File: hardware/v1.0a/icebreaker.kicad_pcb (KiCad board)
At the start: 4 copper layers, 73 x 37 mm, 128 parts, among them J1 Jumper, J10 Jumper, J11 Jumper, J12 Jumper, J13 Jumper, J14 Jumper, J15 Jumper, J16 Jumper, J17 Jumper, J18 Jumper, J19 Jumper, J2 Jumper, J20 Flash, J21 PMOD_1A, J22 PMOD_1B, J23 PMOD_2H, J24 PMOD_2P, J25 RGB Led, J26 5V AUX, J27 5V AUX, J28 CRESET, J3 Jumper, J4 Jumper, J5 Jumper, J6 Jumper, J7 Jumper, J8 Jumper, J9 Jumper, P1 pkl_USB_OTG, P2 UP, P3 UP, P4 UP, P5 UP, SW1 TACT, SW2 TACT, SW3 TACT, SW4 TACT, U1 93C46B-SOT-23-6, U2 3.3V, U3 1V2, U4 FT2232H, U5 W25Q, U6 ICE5LP4K-SG48, U7 12MHz

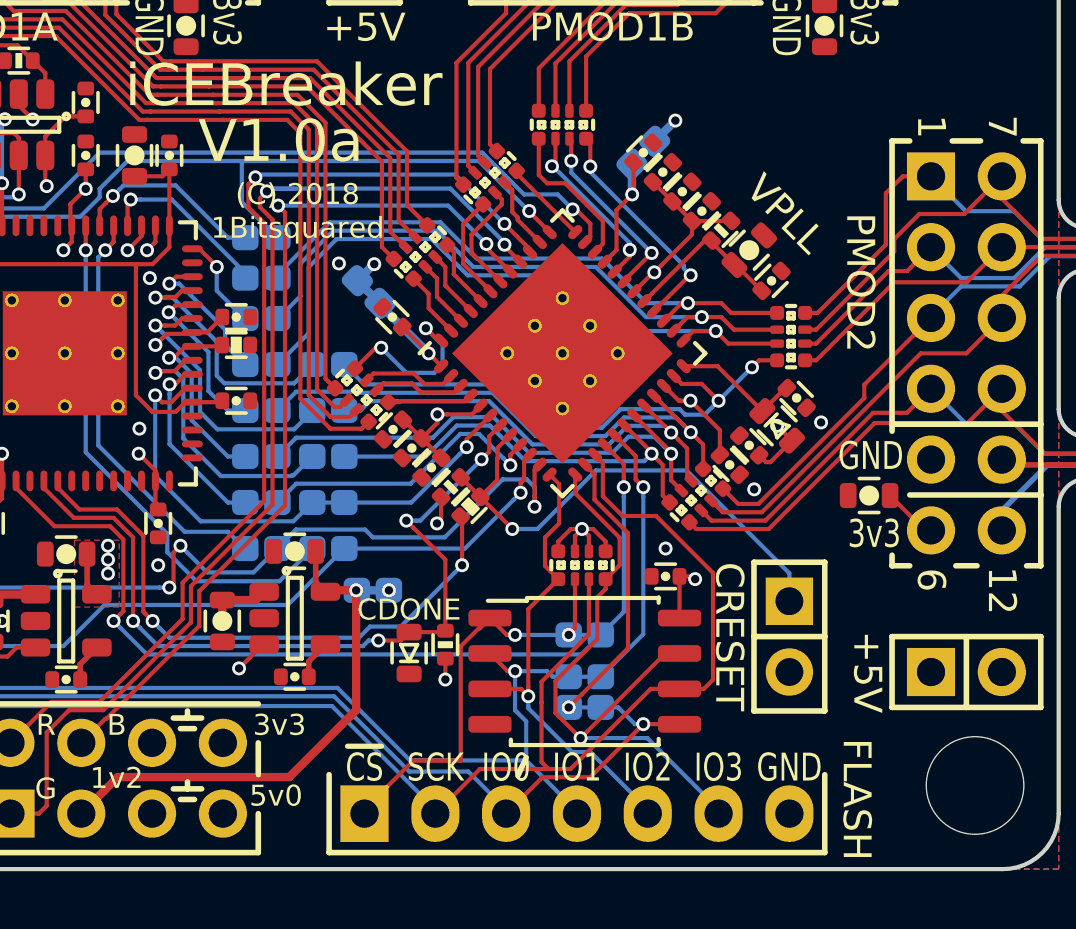
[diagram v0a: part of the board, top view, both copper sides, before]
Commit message: Updated BOM and assembly documentation.
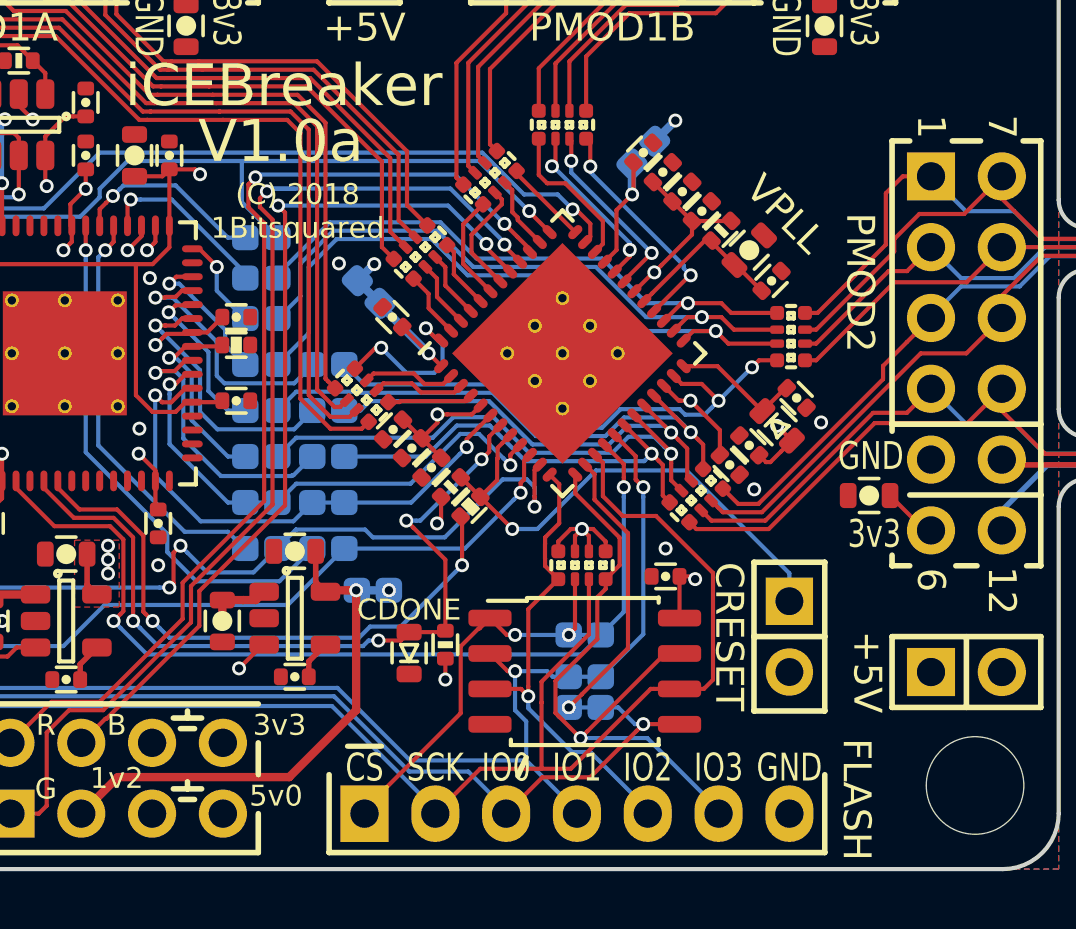
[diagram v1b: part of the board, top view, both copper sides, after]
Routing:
- net +1V8: track 32.5 -> 33.6 mm, vias 0 -> 1
- net /FLASH_CS: track 15.1 -> 14.1 mm

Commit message: Changed the inline CRESET resestor to 2k2.
We need a lower resistor value so that the FTDI chip can reset the FPGA.
Using a 10k resistor results in a voltage divider and the 1.65v is too
high to assert reset.
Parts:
- D3: value GRN -> BLU
- J21: value PMOD_1A -> PMOD
- J22: value PMOD_1B -> PMOD
- J23: value PMOD_2H -> PMOD
- J24: value PMOD_2P -> PMOD
- R26: value 10k -> 2k2
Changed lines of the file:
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@@
       (effects (font (size 1 1) (thickness 0.15)))
     )
-    (fp_text value PMOD_2P (at 2.65 6.35 270) (layer F.Fab)
+    (fp_text value PMOD (at 2.65 6.35 270) (layer F.Fab)
       (effects (font (size 1 1) (thickness 0.15)))
     )
@@
       (effects (font (size 1 1) (thickness 0.15)))
     )
-    (fp_text value PMOD_2H (at 6.45 0.68 90) (layer F.Fab)
+    (fp_text value PMOD (at 6.45 0.68 90) (layer F.Fab)
       (effects (font (size 1 1) (thickness 0.15)))
     )
@@
       (effects (font (size 1 1) (thickness 0.15)))
     )
-    (fp_text value PMOD_1B (at 5.98 0.03 180) (layer F.Fab)
+    (fp_text value PMOD (at 5.98 0.03 180) (layer F.Fab)
       (effects (font (size 1 1) (thickness 0.15)))
     )
@@
       (effects (font (size 1 1) (thickness 0.15)))
     )
-    (fp_text value PMOD_1A (at 6.32 0.03 180) (layer F.Fab)
+    (fp_text value PMOD (at 6.32 0.03 180) (layer F.Fab)
       (effects (font (size 1 1) (thickness 0.15)))
     )
@@
       (effects (font (size 0.635 0.635) (thickness 0.1)))
     )
-    (fp_text value 10k (at -1.838478 0 225) (layer F.Fab)
+    (fp_text value 2k2 (at -1.838478 0 225) (layer F.Fab)
       (effects (font (size 0.635 0.635) (thickness 0.1)))
     )
@@
       (effects (font (size 0.635 0.635) (thickness 0.1)))
     )
-    (fp_text value GRN (at -1.65 0 180) (layer F.Fab)
+    (fp_text value BLU (at -1.65 0 180) (layer F.Fab)
       (effects (font (size 0.5 0.5) (thickness 0.1)))
     )

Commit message: Fixed pin header 3d models.
We had some of the models doubled up or not fully disabled. Now the TH
pin headers are all using KiCad V5 3d model locations and are all
disabled.

This fixes #23
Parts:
- removed the REF** at (42.2, 47.2)
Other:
- board text removed: "1Bitsquared"
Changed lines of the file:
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@@
-(kicad_pcb (version 20171130) (host pcbnew 5.0.0-fee4fd1~66~ubuntu18.04.1)
+(kicad_pcb (version 20171130) (host pcbnew 5.1.2-f72e74a~84~ubuntu18.04.1)
   (general
     (thickness 1.6)
-    (drawings 335)
+    (drawings 334)
     (tracks 1467)
     (zones 0)
-    (modules 128)
+    (modules 127)
     (nets 134)
   )
@@
     (zone_45_only yes)
     (trace_min 0.149)
-    (segment_width 0.2)
-    (edge_width 0.15)
     (via_size 0.5)
     (via_drill 0.3)
@@
     (uvia_min_size 0.2)
     (uvia_min_drill 0.1)
+    (edge_width 0.15)
+    (segment_width 0.2)
     (pcb_text_width 0.3)
     (pcb_text_size 1.5 1.5)
@@
     (aux_axis_origin 0 0)
     (grid_origin 55.1 47.5)
-    (visible_elements FFFFFF7F)
+    (visible_elements FFFFEF7F)
     (pcbplotparams
       (layerselection 0x010fc_ffffffff)
@@
     (pad 7 thru_hole oval (at 0 15.24 90) (size 2.032 1.7272) (drill 1.016) (layers *.Cu *.Mask)
       (net 26 GND))
-    (model Pin_Headers.3dshapes/Pin_Header_Straight_1x07.wrl
-      (offset (xyz 0 -7.619999885559082 0))
+    (model ${KISYS3DMOD}/Connector_PinHeader_2.54mm.3dshapes/PinHeader_1x07_P2.54mm_Vertical.stepX
+      (at (xyz 0 0 0))
       (scale (xyz 1 1 1))
-      (rotate (xyz 0 0 90))
+      (rotate (xyz 0 0 0))
     )
   )
@@
     (pad 8 thru_hole oval (at 2.54 7.62 90) (size 1.7272 1.7272) (drill 1.016) (layers *.Cu *.Mask)
       (net 3 +3V3))
-    (model Pin_Headers.3dshapes/Pin_Header_Straight_2x04.wrl
-      (offset (xyz 1.269999980926514 -3.809999942779541 0))
+    (model ${KISYS3DMOD}/Connector_PinHeader_2.54mm.3dshapes/PinHeader_2x04_P2.54mm_Vertical.stepX
+      (at (xyz 0 0 0))
       (scale (xyz 1 1 1))
-      (rotate (xyz 0 0 90))
+      (rotate (xyz 0 0 0))
     )
   )
@@
     (pad 2 thru_hole oval (at 2.54 0) (size 1.7272 1.7272) (drill 1.016) (layers *.Cu *.Mask)
       (net 26 GND))
-    (model Pin_Headers.3dshapes/Pin_Header_Straight_2x01.wrl
-      (offset (xyz 1.269999980926514 0 0))
+    (model ${KISYS3DMOD}/Connector_PinSocket_2.54mm.3dshapes/PinSocket_1x02_P2.54mm_Vertical.stepX
+      (at (xyz 0 0 0))
       (scale (xyz 1 1 1))
-      (rotate (xyz 0 0 90))
+      (rotate (xyz 0 0 -90))
     )
   )
@@
     (pad 2 thru_hole oval (at 2.54 0 90) (size 1.7272 1.7272) (drill 1.016) (layers *.Cu *.Mask)
       (net 26 GND))
-    (model Pin_Headers.3dshapes/Pin_Header_Straight_2x01.wrl
-      (offset (xyz 1.269999980926514 0 0))
+    (model ${KISYS3DMOD}/Connector_PinSocket_2.54mm.3dshapes/PinSocket_1x02_P2.54mm_Vertical.stepX
+      (at (xyz 0 0 0))
       (scale (xyz 1 1 1))
-      (rotate (xyz 0 0 90))
+      (rotate (xyz 0 0 -90))
     )
   )
@@
     (pad 7 thru_hole oval (at 2.54 12.7 180) (size 1.7272 1.7272) (drill 1.016) (layers *.Cu *.Mask)
       (net 107 /P2_7x))
-    (model Pin_Headers.3dshapes/Pin_Header_Straight_2x06.wrl
-      (offset (xyz 1.269999980926514 -6.349999904632568 0))
+    (model ${KISYS3DMOD}/Connector_PinHeader_2.54mm.3dshapes/PinHeader_2x06_P2.54mm_Horizontal.stepX
+      (at (xyz 0 0 0))
       (scale (xyz 1 1 1))
-      (rotate (xyz 0 0 90))
+      (rotate (xyz 0 0 0))
     )
   )
@@
     (pad 7 thru_hole oval (at 12.7 2.54 90) (size 1.7272 1.7272) (drill 1.016) (layers *.Cu *.Mask)
       (net 107 /P2_7x))
-    (model Socket_Strips.3dshapes/Socket_Strip_Straight_2x06.wrl
-      (offset (xyz 6.349999904632568 -1.269999980926514 0))
+    (model ${KISYS3DMOD}/Connector_PinSocket_2.54mm.3dshapes/PinSocket_2x06_P2.54mm_Horizontal.stepX
+      (at (xyz 0 0 0))
       (scale (xyz 1 1 1))
-      (rotate (xyz 0 0 180))
+      (rotate (xyz 0 0 -90))
     )
   )
@@
     (pad 6 thru_hole circle (at 0 0 180) (size 1.7272 1.7272) (drill 1.016) (layers *.Cu *.Mask)
       (net 3 +3V3))
-    (model dis${KISYS3DMOD}/Connector_PinSocket_2.54mm.3dshapes/PinSocket_2x06_P2.54mm_Horizontal.step
+    (model ${KISYS3DMOD}/Connector_PinSocket_2.54mm.3dshapes/PinSocket_2x06_P2.54mm_Horizontal.stepX
       (at (xyz 0 0 0))
       (scale (xyz 1 1 1))
@@
     (pad 7 thru_hole oval (at 12.7 2.54 180) (size 1.7272 1.7272) (drill 1.016) (layers *.Cu *.Mask)
       (net 93 /P1A7x))
-    (model dis${KISYS3DMOD}/Connector_PinSocket_2.54mm.3dshapes/PinSocket_2x06_P2.54mm_Horizontal.step
-      (offset (xyz 6.35 -1.27 0))
+    (model ${KISYS3DMOD}/Connector_PinSocket_2.54mm.3dshapes/PinSocket_2x06_P2.54mm_Horizontal.stepX
+      (at (xyz 0 0 0))
       (scale (xyz 1 1 1))
       (rotate (xyz 0 0 -90))
@@
       (net 6 /xFIFO_WKUP))
   )
-  (module pkl_logos:1b2_Logo_SilkS_5mm locked (layer B.Cu)
-    (at 42.2 47.2 180)
-    (fp_text reference REF** (at 0 -4 180) (layer B.Fab) hide
-      (effects (font (size 1 1) (thickness 0.15)) (justify mirror))
-    )
-    (fp_text value 1b2_Logo_SilkS_5mm (at 0 4 180) (layer B.Fab) hide
-      (effects (font (size 1 1) (thickness 0.15)) (justify mirror))
-    )
-    (fp_line (start -0.5 0.5) (end -0.5 2.5) (layer B.SilkS) (width 0.2))
-    (fp_line (start -0.5 2.5) (end -2.5 2.5) (layer B.SilkS) (width 0.2))
-    (fp_line (start -2.5 2.5) (end -2.5 0.5) (layer B.SilkS) (width 0.2))
-    (fp_line (start -2.5 0.5) (end -0.5 0.5) (layer B.SilkS) (width 0.2))
-    (fp_line (start -0.5 2.5) (end 0 2) (layer B.SilkS) (width 0.2))
-    (fp_line (start 0 2) (end 0 0) (layer B.SilkS) (width 0.2))
-    (fp_line (start 0 0) (end -0.5 0.5) (layer B.SilkS) (width 0.2))
-    (fp_line (start -2.5 0.5) (end -2 0) (layer B.SilkS) (width 0.2))
-    (fp_line (start -2 0) (end 0 0) (layer B.SilkS) (width 0.2))
-    (fp_line (start 2 2) (end 0.5 2) (layer B.SilkS) (width 0.2))
-    (fp_line (start 0.5 2) (end 0.5 -0.5) (layer B.SilkS) (width 0.2))
-    (fp_line (start 0.5 -0.5) (end -2 -0.5) (layer B.SilkS) (width 0.2))
-    (fp_line (start -2 -0.5) (end -2 -2) (layer B.SilkS) (width 0.2))
-    (fp_line (start -2 -2) (end 2 -2) (layer B.SilkS) (width 0.2))
-    (fp_line (start 2 -2) (end 2 2) (layer B.SilkS) (width 0.2))
-    (fp_line (start 2 2) (end 2.5 1.5) (layer B.SilkS) (width 0.2))
-    (fp_line (start 2.5 1.5) (end 2.5 -2.5) (layer B.SilkS) (width 0.2))
-    (fp_line (start 2.5 -2.5) (end 2 -2) (layer B.SilkS) (width 0.2))
-    (fp_line (start -2 -2) (end -1.5 -2.5) (layer B.SilkS) (width 0.2))
-    (fp_line (start -1.5 -2.5) (end 2.5 -2.5) (layer B.SilkS) (width 0.2))
-  )
   (module pkl_dipol:R_Array_Convex_4x0402 (layer F.Cu)
     (at 57.105546 43.866206 135)
@@
     (pad 2 smd roundrect (at 0.75 0 90) (size 0.6 0.9) (layers F.Cu F.Paste F.Mask) (roundrect_rratio 0.25)
       (net 3 +3V3))
-    (model ${KISYS3DMOD}/Capacitor_SMD.3dshapes/C_0603_1608Metric.step
+    (model ${KISYS3DMOD}/Capacitor_SMD.3dshapes/C_0603_1608Metric.stepX
       (at (xyz 0 0 0))
       (scale (xyz 1 1 1))
@@
     (pad 1 smd roundrect (at -0.75 0 90) (size 0.6 0.9) (layers F.Cu F.Paste F.Mask) (roundrect_rratio 0.25)
       (net 26 GND))
-    (model ${KISYS3DMOD}/Capacitor_SMD.3dshapes/C_0603_1608Metric.step
+    (model ${KISYS3DMOD}/Capacitor_SMD.3dshapes/C_0603_1608Metric.stepX
       (at (xyz 0 0 0))
       (scale (xyz 1 1 1))
@@
     (pad 2 smd roundrect (at 0.75 0) (size 0.6 0.9) (layers F.Cu F.Paste F.Mask) (roundrect_rratio 0.25)
       (net 3 +3V3))
-    (model ${KISYS3DMOD}/Capacitor_SMD.3dshapes/C_0603_1608Metric.step
+    (model ${KISYS3DMOD}/Capacitor_SMD.3dshapes/C_0603_1608Metric.stepX
       (at (xyz 0 0 0))
       (scale (xyz 1 1 1))
@@
     (effects (font (size 0.75 0.75) (thickness 0.1875)))
   )
-  (gr_text 1Bitsquared (at 42.1 51) (layer B.SilkS)
-    (effects (font (size 1 1) (thickness 0.25)) (justify mirror))
-  )
   (gr_text CDONE (at 56.7 56.7) (layer F.SilkS)

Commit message: Added more legend silkscreen to ears.
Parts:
- added REF**: 1b2_Logo_SilkS_5mm, pkl_logos:1b2_Logo_SilkS_5mm, B.Cu at (42.2, 47.2)
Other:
- board text added: "1Bitsquared"
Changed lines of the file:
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@@
   (general
     (thickness 1.6)
-    (drawings 334)
+    (drawings 335)
     (tracks 1467)
     (zones 0)
-    (modules 127)
+    (modules 128)
     (nets 134)
   )
@@
     (add_net "Net-(U7-Pad2)")
   )
+  (module pkl_logos:1b2_Logo_SilkS_5mm locked (layer B.Cu)
+    (at 42.2 47.2 180)
+    (fp_text reference REF** (at 0 -4 180) (layer B.Fab) hide
+      (effects (font (size 1 1) (thickness 0.15)) (justify mirror))
+    )
+    (fp_text value 1b2_Logo_SilkS_5mm (at 0 4 180) (layer B.Fab) hide
+      (effects (font (size 1 1) (thickness 0.15)) (justify mirror))
+    )
+    (fp_line (start -0.5 0.5) (end -0.5 2.5) (layer B.SilkS) (width 0.2))
+    (fp_line (start -0.5 2.5) (end -2.5 2.5) (layer B.SilkS) (width 0.2))
+    (fp_line (start -2.5 2.5) (end -2.5 0.5) (layer B.SilkS) (width 0.2))
+    (fp_line (start -2.5 0.5) (end -0.5 0.5) (layer B.SilkS) (width 0.2))
+    (fp_line (start -0.5 2.5) (end 0 2) (layer B.SilkS) (width 0.2))
+    (fp_line (start 0 2) (end 0 0) (layer B.SilkS) (width 0.2))
+    (fp_line (start 0 0) (end -0.5 0.5) (layer B.SilkS) (width 0.2))
+    (fp_line (start -2.5 0.5) (end -2 0) (layer B.SilkS) (width 0.2))
+    (fp_line (start -2 0) (end 0 0) (layer B.SilkS) (width 0.2))
+    (fp_line (start 2 2) (end 0.5 2) (layer B.SilkS) (width 0.2))
+    (fp_line (start 0.5 2) (end 0.5 -0.5) (layer B.SilkS) (width 0.2))
+    (fp_line (start 0.5 -0.5) (end -2 -0.5) (layer B.SilkS) (width 0.2))
+    (fp_line (start -2 -0.5) (end -2 -2) (layer B.SilkS) (width 0.2))
+    (fp_line (start -2 -2) (end 2 -2) (layer B.SilkS) (width 0.2))
+    (fp_line (start 2 -2) (end 2 2) (layer B.SilkS) (width 0.2))
+    (fp_line (start 2 2) (end 2.5 1.5) (layer B.SilkS) (width 0.2))
+    (fp_line (start 2.5 1.5) (end 2.5 -2.5) (layer B.SilkS) (width 0.2))
+    (fp_line (start 2.5 -2.5) (end 2 -2) (layer B.SilkS) (width 0.2))
+    (fp_line (start -2 -2) (end -1.5 -2.5) (layer B.SilkS) (width 0.2))
+    (fp_line (start -1.5 -2.5) (end 2.5 -2.5) (layer B.SilkS) (width 0.2))
+  )
   (module Pin_Headers:Pin_Header_Straight_1x07 locked (layer F.Cu)
     (at 55.1 64.01 90)
@@
     )
   )
+  (gr_text 1Bitsquared (at 42.1 51) (layer B.SilkS)
+    (effects (font (size 1 1) (thickness 0.25)) (justify mirror))
+  )
   (gr_line (start 59.8 62.3) (end 59.45 61.8) (layer B.SilkS) (width 0.2))

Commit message: Replaced/added the null logo to the boards.
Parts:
- REF**: value 1b2_Logo_SilkS_5mm -> null_Logo_SilkS_5mm; footprint pkl_logos:1b2_Logo_SilkS_5mm -> pkl_logos:null_Logo_SilkS_5mm
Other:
- board text added: "NULL"
- board text removed: "1Bitsquared"
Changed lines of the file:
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@@
-(kicad_pcb (version 20171130) (host pcbnew 5.1.2-f72e74a~84~ubuntu18.04.1)
+(kicad_pcb (version 20171130) (host pcbnew 5.1.5-52549c5~86~ubuntu19.10.1)
   (general
     (thickness 1.6)
@@
     (add_net "Net-(U7-Pad2)")
   )
-  (module pkl_logos:1b2_Logo_SilkS_5mm locked (layer B.Cu)
+  (module pkl_logos:null_Logo_SilkS_5mm locked (layer B.Cu)
     (at 42.2 47.2 180)
     (fp_text reference REF** (at 0 -4 180) (layer B.Fab) hide
       (effects (font (size 1 1) (thickness 0.15)) (justify mirror))
     )
-    (fp_text value 1b2_Logo_SilkS_5mm (at 0 4 180) (layer B.Fab) hide
+    (fp_text value null_Logo_SilkS_5mm (at 0 4 180) (layer B.Fab) hide
       (effects (font (size 1 1) (thickness 0.15)) (justify mirror))
     )
-    (fp_line (start -0.5 0.5) (end -0.5 2.5) (layer B.SilkS) (width 0.2))
-    (fp_line (start -0.5 2.5) (end -2.5 2.5) (layer B.SilkS) (width 0.2))
-    (fp_line (start -2.5 2.5) (end -2.5 0.5) (layer B.SilkS) (width 0.2))
-    (fp_line (start -2.5 0.5) (end -0.5 0.5) (layer B.SilkS) (width 0.2))
-    (fp_line (start -0.5 2.5) (end 0 2) (layer B.SilkS) (width 0.2))
-    (fp_line (start 0 2) (end 0 0) (layer B.SilkS) (width 0.2))
-    (fp_line (start 0 0) (end -0.5 0.5) (layer B.SilkS) (width 0.2))
-    (fp_line (start -2.5 0.5) (end -2 0) (layer B.SilkS) (width 0.2))
-    (fp_line (start -2 0) (end 0 0) (layer B.SilkS) (width 0.2))
-    (fp_line (start 2 2) (end 0.5 2) (layer B.SilkS) (width 0.2))
-    (fp_line (start 0.5 2) (end 0.5 -0.5) (layer B.SilkS) (width 0.2))
-    (fp_line (start 0.5 -0.5) (end -2 -0.5) (layer B.SilkS) (width 0.2))
-    (fp_line (start -2 -0.5) (end -2 -2) (layer B.SilkS) (width 0.2))
-    (fp_line (start -2 -2) (end 2 -2) (layer B.SilkS) (width 0.2))
-    (fp_line (start 2 -2) (end 2 2) (layer B.SilkS) (width 0.2))
-    (fp_line (start 2 2) (end 2.5 1.5) (layer B.SilkS) (width 0.2))
-    (fp_line (start 2.5 1.5) (end 2.5 -2.5) (layer B.SilkS) (width 0.2))
-    (fp_line (start 2.5 -2.5) (end 2 -2) (layer B.SilkS) (width 0.2))
-    (fp_line (start -2 -2) (end -1.5 -2.5) (layer B.SilkS) (width 0.2))
-    (fp_line (start -1.5 -2.5) (end 2.5 -2.5) (layer B.SilkS) (width 0.2))
+    (fp_arc (start -0.4 -0.2) (end -0.7 -0.2) (angle 180) (layer B.SilkS) (width 0.15))
+    (fp_line (start 1 -0.5) (end 1.5 -0.5) (layer B.SilkS) (width 0.15))
+    (fp_line (start 1 0.5) (end 1 -0.5) (layer B.SilkS) (width 0.15))
+    (fp_line (start 0.2 -0.5) (end 0.7 -0.5) (layer B.SilkS) (width 0.15))
+    (fp_line (start 0.2 0.5) (end 0.2 -0.5) (layer B.SilkS) (width 0.15))
+    (fp_line (start -0.1 0.5) (end -0.1 -0.2) (layer B.SilkS) (width 0.15))
+    (fp_line (start -0.7 0.5) (end -0.7 -0.2) (layer B.SilkS) (width 0.15))
+    (fp_line (start -1 -0.5) (end -1 0.5) (layer B.SilkS) (width 0.15))
+    (fp_line (start -1.5 0.5) (end -1 -0.5) (layer B.SilkS) (width 0.15))
+    (fp_line (start -1.5 -0.5) (end -1.5 0.5) (layer B.SilkS) (width 0.15))
+    (fp_line (start 2.5 2.5) (end -2.5 2.5) (layer B.SilkS) (width 0.2))
+    (fp_line (start -2.5 2.5) (end -2.5 -2.5) (layer B.SilkS) (width 0.2))
+    (fp_line (start 2.5 2.5) (end 2.5 -2.5) (layer B.SilkS) (width 0.2))
+    (fp_line (start -2.5 -2.5) (end 2.5 -2.5) (layer B.SilkS) (width 0.2))
   )
   (module Pin_Headers:Pin_Header_Straight_1x07 locked (layer F.Cu)
@@
     )
   )
-  (gr_text 1Bitsquared (at 42.1 51) (layer B.SilkS)
+  (gr_text NULL (at 42.1 51) (layer B.SilkS)
     (effects (font (size 1 1) (thickness 0.25)) (justify mirror))
   )
